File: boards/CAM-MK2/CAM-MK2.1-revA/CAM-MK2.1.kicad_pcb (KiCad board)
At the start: 4 copper layers, 40 x 40 mm, 104 parts, among them J101 USB4105-GF-A, J102 2157601002, J103 Conn_01x03, J104 Conn_01x05, J105 Conn_01x03, J106 Conn_01x05, J107 Conn_01x03, J108 Conn_01x03, J109 Conn_01x03, Q101 DMNH6022SSDQ, U101 ECMF02-2AMX6, U102 MCP2518FDT-xSL, U103 TPSM863252, U104 TPS61288, U105 TCAN337G, U106 INA745x, U107 74LVC2G157, U108 TPS2121, U109 ESP32-S3-MINI-1U, Y101 40MHz

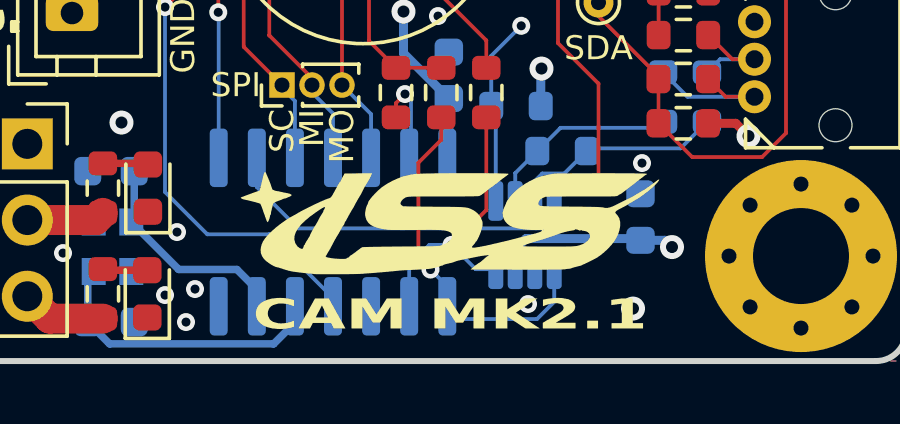
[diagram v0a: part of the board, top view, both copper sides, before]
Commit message: Fixed Schematic Linking
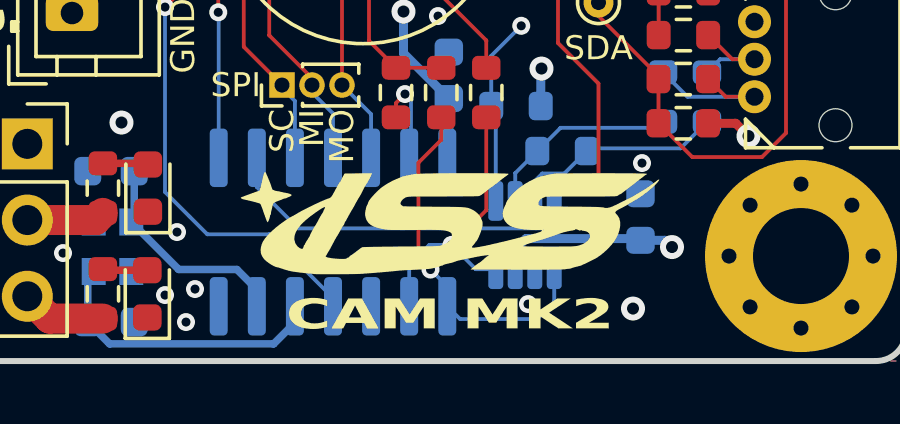
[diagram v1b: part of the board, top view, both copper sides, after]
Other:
- board text added: "CAM MK2"
- board text removed: "CAM MK2.1"
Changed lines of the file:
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@@
 	(paper "A4")
 	(title_block
-		(title "Stargazer Camera Board MK2.1")
+		(title "Stargazer Camera Board MK2")
 		(date "2024-12-01")
 		(rev "A")
@@
 		)
 	)
-	(gr_text "CAM MK2.1"
+	(gr_text "CAM MK2"
 		(at 154.8 108.45 0)
 		(layer "F.SilkS")
@@
 			)
 		)
-		(render_cache "CAM MK2.1" 0
+		(render_cache "CAM MK2" 0
 			(polygon
 				(pts
-					(xy 151.998046 108.779759) (xy 151.980643 108.828289) (xy 151.921961 108.858257) (xy 151.850767 108.865)
-					(xy 151.347749 108.865) (xy 151.272208 108.856675) (xy 151.215832 108.820964) (xy 151.204501 108.779759)
-					(xy 151.204501 107.871664) (xy 151.221427 107.823133) (xy 151.285078 107.791751) (xy 151.347749 107.786423)
-					(xy 151.850767 107.786423) (xy 151.928434 107.794747) (xy 151.986396 107.830459) (xy 151.998046 107.871664)
-					(xy 151.998046 108.145949) (xy 151.758077 108.145949) (xy 151.758077 107.942739) (xy 151.445935 107.942739)
-					(xy 151.445935 108.708684) (xy 151.758077 108.708684) (xy 151.758077 108.505474) (xy 151.998046 108.505474)
+					(xy 152.436951 108.779759) (xy 152.419548 108.828289) (xy 152.360866 108.858257) (xy 152.289672 108.865)
+					(xy 151.786654 108.865) (xy 151.711113 108.856675) (xy 151.654737 108.820964) (xy 151.643406 108.779759)
+					(xy 151.643406 107.871664) (xy 151.660332 107.823133) (xy 151.723983 107.791751) (xy 151.786654 107.786423)
+					(xy 152.289672 107.786423) (xy 152.367339 107.794747) (xy 152.425301 107.830459) (xy 152.436951 107.871664)
+					(xy 152.436951 108.145949) (xy 152.196982 108.145949) (xy 152.196982 107.942739) (xy 151.88484 107.942739)
+					(xy 151.88484 108.708684) (xy 152.196982 108.708684) (xy 152.196982 108.505474) (xy 152.436951 108.505474)
 				)
 			)
 			(polygon
 				(pts
-					(xy 152.999319 108.865) (xy 152.760083 108.865) (xy 152.711723 108.677421) (xy 152.409839 108.677421)
-					(xy 152.361479 108.865) (xy 152.123342 108.865) (xy 152.123342 108.862313) (xy 152.222335 108.521106)
-					(xy 152.441713 108.521106) (xy 152.677651 108.521106) (xy 152.560415 108.035795) (xy 152.441713 108.521106)
-					(xy 152.222335 108.521106) (xy 152.435485 107.786423) (xy 152.689009 107.786423)
+					(xy 153.438224 108.865) (xy 153.198988 108.865) (xy 153.150628 108.677421) (xy 152.848744 108.677421)
+					(xy 152.800384 108.865) (xy 152.562247 108.865) (xy 152.562247 108.862313) (xy 152.66124 108.521106)
+					(xy 152.880618 108.521106) (xy 153.116556 108.521106) (xy 152.99932 108.035795) (xy 152.880618 108.521106)
+					(xy 152.66124 108.521106) (xy 152.87439 107.786423) (xy 153.127914 107.786423)
 				)
 			)
 			(polygon
 				(pts
-					(xy 154.103541 108.865) (xy 153.871633 108.865) (xy 153.871633 108.328886) (xy 153.875296 108.278267)
-					(xy 153.882852 108.229323) (xy 153.886287 108.210917) (xy 153.677826 108.755579) (xy 153.55546 108.755579)
-					(xy 153.346266 108.210917) (xy 153.354401 108.259679) (xy 153.359871 108.3093) (xy 153.360554 108.328886)
-					(xy 153.360554 108.865) (xy 153.128646 108.865) (xy 153.128646 107.786423) (xy 153.356524 107.786423)
-					(xy 153.610048 108.376025) (xy 153.616277 108.424385) (xy 153.622505 108.376025) (xy 153.875663 107.786423)
-					(xy 154.103541 107.786423)
+					(xy 154.542446 108.865) (xy 154.310538 108.865) (xy 154.310538 108.328886) (xy 154.314201 108.278267)
+					(xy 154.321757 108.229323) (xy 154.325192 108.210917) (xy 154.116731 108.755579) (xy 153.994365 108.755579)
+					(xy 153.785171 108.210917) (xy 153.793306 108.259679) (xy 153.798776 108.3093) (xy 153.799459 108.328886)
+					(xy 153.799459 108.865) (xy 153.567551 108.865) (xy 153.567551 107.786423) (xy 153.795429 107.786423)
+					(xy 154.048953 108.376025) (xy 154.055182 108.424385) (xy 154.06141 108.376025) (xy 154.314568 107.786423)
+					(xy 154.542446 107.786423)
 				)
 			)
 			(polygon
 				(pts
-					(xy 155.696493 108.865) (xy 155.464584 108.865) (xy 155.464584 108.328886) (xy 155.468248 108.278267)
-					(xy 155.475804 108.229323) (xy 155.479239 108.210917) (xy 155.270778 108.755579) (xy 155.148412 108.755579)
-					(xy 154.939218 108.210917) (xy 154.947353 108.259679) (xy 154.952823 108.3093) (xy 154.953506 108.328886)
-					(xy 154.953506 108.865) (xy 154.721598 108.865) (xy 154.721598 107.786423) (xy 154.949476 107.786423)
-					(xy 155.203 108.376025) (xy 155.209229 108.424385) (xy 155.215457 108.376025) (xy 155.468614 107.786423)
-					(xy 155.696493 107.786423)
+					(xy 156.135398 108.865) (xy 155.903489 108.865) (xy 155.903489 108.328886) (xy 155.907153 108.278267)
+					(xy 155.914709 108.229323) (xy 155.918144 108.210917) (xy 155.709683 108.755579) (xy 155.587317 108.755579)
+					(xy 155.378123 108.210917) (xy 155.386258 108.259679) (xy 155.391728 108.3093) (xy 155.392411 108.328886)
+					(xy 155.392411 108.865) (xy 155.160503 108.865) (xy 155.160503 107.786423) (xy 155.388381 107.786423)
+					(xy 155.641905 108.376025) (xy 155.648134 108.424385) (xy 155.654362 108.376025) (xy 155.907519 107.786423)
+					(xy 156.135398 107.786423)
 				)
 			)
 			(polygon
 				(pts
-					(xy 156.695202 108.865) (xy 156.429588 108.865) (xy 156.123674 108.387749) (xy 156.123674 108.865)
-					(xy 155.88224 108.865) (xy 155.88224 107.786423) (xy 156.123674 107.786423) (xy 156.123674 108.246821)
-					(xy 156.391486 107.786423) (xy 156.655268 107.786423) (xy 156.655268 107.793995) (xy 156.327372 108.31008)
+					(xy 157.134107 108.865) (xy 156.868493 108.865) (xy 156.562579 108.387749) (xy 156.562579 108.865)
+					(xy 156.321145 108.865) (xy 156.321145 107.786423) (xy 156.562579 107.786423) (xy 156.562579 108.246821)
+					(xy 156.830391 107.786423) (xy 157.094173 107.786423) (xy 157.094173 107.793995) (xy 156.766277 108.31008)
 				)
 			)
 			(polygon
 				(pts
-					(xy 157.544068 108.080247) (xy 157.532557 108.13029) (xy 157.503957 108.177567) (xy 157.491678 108.192843)
-					(xy 157.048377 108.708684) (xy 157.54187 108.708684) (xy 157.54187 108.865) (xy 156.759682 108.865)
-					(xy 156.759682 108.763394) (xy 157.305931 108.123234) (xy 157.305931 107.942739) (xy 157.012107 107.942739)
-					(xy 157.012107 108.130317) (xy 156.776168 108.130317) (xy 156.776168 107.871664) (xy 156.793572 107.823133)
-					(xy 156.852253 107.793166) (xy 156.923447 107.786423) (xy 157.396423 107.786423) (xy 157.474283 107.794747)
-					(xy 157.532389 107.830459) (xy 157.544068 107.871664)
-				)
-			)
-			(polygon
-				(pts
-					(xy 157.92472 108.865) (xy 157.692812 108.865) (xy 157.692812 108.693053) (xy 157.92472 108.693053)
-				)
-			)
-			(polygon
-				(pts
-					(xy 158.388171 108.865) (xy 158.151134 108.865) (xy 158.151134 108.099054) (xy 158.058443 108.099054)
-					(xy 158.058443 108.075607) (xy 158.183374 107.786423) (xy 158.388171 107.786423)
+					(xy 157.982973 108.080247) (xy 157.971462 108.13029) (xy 157.942862 108.177567) (xy 157.930583 108.192843)
+					(xy 157.487282 108.708684) (xy 157.980775 108.708684) (xy 157.980775 108.865) (xy 157.198587 108.865)
+					(xy 157.198587 108.763394) (xy 157.744836 108.123234) (xy 157.744836 107.942739) (xy 157.451012 107.942739)
+					(xy 157.451012 108.130317) (xy 157.215073 108.130317) (xy 157.215073 107.871664) (xy 157.232477 107.823133)
+					(xy 157.291158 107.793166) (xy 157.362352 107.786423) (xy 157.835328 107.786423) (xy 157.913188 107.794747)
+					(xy 157.971294 107.830459) (xy 157.982973 107.871664)
 				)
 			)

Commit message: CAM MK2.1 Routing
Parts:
- removed Q101: DMNH6022SSDQ, Package_SO:SO-8_3.9x4.9mm_P1.27mm
- added C123: 0.1uF, Capacitor_SMD:C_0603_1608Metric, B.Cu at (138.2, 87.3)
- added C124: 0.1uF, Capacitor_SMD:C_0603_1608Metric, B.Cu at (138.2, 90.2)
- added C125: 22nF, Capacitor_SMD:C_0603_1608Metric, B.Cu at (139.2, 97.3)
- added C126: 22nF, Capacitor_SMD:C_0603_1608Metric, B.Cu at (136.7, 87.3)
- added C127: 22nF, Capacitor_SMD:C_0603_1608Metric, B.Cu at (136.7, 81.5)
- added C128: 0.1uF, Capacitor_SMD:C_0603_1608Metric, B.Cu at (133.1, 85.9)
- added R103: 10k, Resistor_SMD:R_0603_1608Metric, F.Cu at (138.2, 84.2)
- added R104: 10k, Resistor_SMD:R_0603_1608Metric, F.Cu at (142.0, 71.5)
- added R147: 10k, Resistor_SMD:R_0603_1608Metric, F.Cu at (141.8, 79.8)
- added R148: 680, Resistor_SMD:R_0603_1608Metric, B.Cu at (144.6, 90.2)
- added R149: 10k, Resistor_SMD:R_0603_1608Metric, B.Cu at (142.0, 73.9)
- added U111: TPS274160B, Package_WQFN:WQFN-RLH0028A, B.Cu at (141.4, 88.8)
- R115: value 470 -> 3.3k
- R132, R134: value 1k -> 220; moved to F.Cu
- R133, R135: value 3.3k -> 220; moved to F.Cu
- U107: value 74LVC2G157 -> ADG752BRT; footprint Package_SO:VSSOP-8_2.3x2mm_P0.5mm -> Package_TO_SOT_SMD:SOT-23-6
- moved R134 5.46 mm to (141.3, 88.7), turned to 0 degrees
- moved R135 3.34 mm to (141.3, 87.2), turned to 0 degrees
- moved R133 1.15 mm to (141.3, 84.2), turned to 0 degrees
- moved R132 1.05 mm to (141.3, 85.8), turned to 0 degrees
- moved U107 0.80 mm to (132.8, 88.7), turned to -90 degrees
- moved C120 0.47 mm to (161.8, 71.9)
- moved R140 0.47 mm to (161.8, 74.9)
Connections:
- J104 pad 3: +12V -> /CAM_1_POW
- J104 pad 4: /TX_1 -> Net-(J104-Pin_4)
- J104 pad 5: /RX_1 -> Net-(J104-Pin_5)
- J105 pad 1: +12V -> /VTX_POW
- J105 pad 2: /VTX_POW -> GND
- J106 pad 1: /CAM_2_POW -> GND
- J106 pad 3: +12V -> /CAM_2_POW
- J106 pad 4: /TX_2 -> Net-(J106-Pin_4)
- J106 pad 5: /RX_2 -> Net-(J106-Pin_5)
- J107 pad 1: GND -> /BOOT_SW
- J107 pad 3: /BOOT_SW -> GND
- J109 pad 2: /SPI_MISO -> /SPI_MOSI
- J109 pad 3: /SPI_MOSI -> /SPI_MISO
- R132 pad 1: Net-(Q101A-G1) -> Net-(J104-Pin_5)
- R132 pad 2: /ON_OFF_VTX -> /RX_1
- R133 pad 1: /ON_OFF_VTX -> Net-(J104-Pin_4)
- R133 pad 2: GND -> /TX_1
- R134 pad 1: Net-(Q101B-G2) -> Net-(J106-Pin_5)
- R134 pad 2: /ON_OFF_2 -> /RX_2
- R135 pad 1: /ON_OFF_2 -> Net-(J106-Pin_4)
- R135 pad 2: GND -> /TX_2
- U102 pad 11: /SPI_MISO -> /SPI_MOSI
- U102 pad 12: /SPI_MOSI -> /SPI_MISO
- U104 pad 6: /12V_EN -> Net-(U104-EN)
- U107 pad 1: /VIDEO_1 -> /VIDEO_OUT
- U107 pad 2: /VIDEO_2 -> +3V3
- U107 pad 3: unconnected-(U107-~{Y}-Pad3) -> /VIDEO_1
- U107 pad 4: GND -> /VIDEO_SELECT
- U107 pad 5: /VIDEO_OUT -> GND
- U107 pad 6: /VIDEO_SELECT -> /VIDEO_2
- U109 pad 19: /SPI_MISO -> /SPI_MOSI
- U109 pad 20: /SPI_MOSI -> /SPI_MISO
- U109 pad 40: /12V_EN -> /ON_OFF_1
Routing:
- net /ON_OFF_1: track 0.00 -> 30.4 mm
- net /12V_EN: track 28.9 -> 0.00 mm, vias 1 -> 0
- net Net-(U111-EN2): track 0.00 -> 19.9 mm, vias 0 -> 1
- net /TX_2: track 18.6 -> 5.06 mm
- net /RX_2: track 18.5 -> 5.29 mm
- net Net-(J106-Pin_4): track 0.00 -> 12.9 mm
- net Net-(J106-Pin_5): track 0.00 -> 12.6 mm
- net Net-(U111-EN3): track 0.00 -> 10.6 mm, vias 0 -> 1
- net +12V: track 53.0 -> 43.8 mm, vias 2 -> 3
- net /TX_1: track 12.9 -> 3.81 mm
- net /RX_1: track 13.0 -> 4.09 mm
- net Net-(Q101B-G2): track 7.81 -> 0.00 mm
- net Net-(J104-Pin_4): track 0.00 -> 7.43 mm
- net Net-(J104-Pin_5): track 0.00 -> 7.32 mm
- net /ON_OFF_2: track 11.1 -> 3.80 mm, vias 1 -> 0
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- removed copper zone on B.Cu, net /CAM_2_POW
- removed copper zone on B.Cu, net /VTX_POW
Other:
- board text added: "SYS PWR"
- board text removed: "SYS POWER"

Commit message: More CAM MK2.1 Routing
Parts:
- moved R104 7.95 mm to (141.7, 79.4)
- moved C121 2.00 mm to (142.6, 73.2), turned to 90 degrees
- moved C122 2.00 mm to (141.1, 73.2), turned to 90 degrees
- moved R147 1.85 mm to (141.7, 77.9)
- moved R149 1.51 mm to (141.8, 72.4)
- moved C124 1.06 mm to (137.4, 89.5), turned to 180 degrees
- moved C128 0.50 mm to (132.6, 85.9)
- moved U107 0.29 mm to (132.6, 88.7)
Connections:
- U109 pad 40: /ON_OFF_1 -> unconnected-(U109-RXD0-Pad40)
- U109 pad 7: unconnected-(U109-IO3-Pad7) -> /ON_OFF_1
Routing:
- net /ON_OFF_1: track 30.4 -> 3.16 mm
- net Net-(U111-EN2): track 19.9 -> 11.2 mm
- net Net-(U111-EN3): track 10.6 -> 13.2 mm
- net +3V3: track 40.0 -> 42.1 mm
- net Net-(U104-EN): track 1.45 -> 3.02 mm
- net +12V: track 43.8 -> 45.2 mm, vias 3 -> 4
- net /VIDEO_SELECT: track 19.9 -> 21.0 mm
- net /ON_OFF_2: track 3.80 -> 2.89 mm
- net GND: vias 66 -> 68
